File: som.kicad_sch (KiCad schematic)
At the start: 29 parts, among them J15 Bus_DDR4_SODIMM_CUSTOM_Jetson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, M1 Jetson-Orin-NX-Nano, U4 NTS0102_XSON

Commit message: Init commit
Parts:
- C1, C2: LCSC Part # (none) -> C696814
- C40, C41: LCSC Part # (none) -> C85960
- D34: LCSC Part # (none) -> C145179
- D55: LCSC Part # (none) -> C5182093
- FB1: LCSC Part # (none) -> ---
- J15: LCSC Part # (none) -> C2766246
- R1, R11, R12, R2, R3, R4, R5: LCSC Part # (none) -> C242160
- R294: LCSC Part # (none) -> C2076845
- R80: LCSC Part # (none) -> C2076851
- S1: LCSC Part # (none) -> C221676
- U4: LCSC Part # (none) -> C2687851

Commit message: Add field Digikey Part Number. Add Chinese substitute components
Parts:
- BT1: Digikey Part # (none) -> 728-1057-ND
- C1, C2: Digikey Part # (none) -> 399-13128-1-ND
- C40, C41: Digikey Part # (none) -> 490-10697-1-ND
- D34: Digikey Part # (none) -> RB521S30T1GOSCT-ND
- D55: Digikey Part # (none) -> 296-47864-1-ND
- FB1: Digikey Part # (none) -> 732-6128-1-ND; LCSC Part # --- -> (none)
- H1, H2: Digikey Part # (none) -> 732-9774065151RCT-ND
- J15: Digikey Part # (none) -> A126764CT-ND
- R1, R11, R12, R2, R3, R4, R5: Digikey Part # (none) -> P0.0JCT-ND
- R294: Digikey Part # (none) -> CR0402-FX-2201GLFCT-ND
- R80: Digikey Part # (none) -> CR0402-FX-4701GLFCT-ND
- S1: Digikey Part # (none) -> CKN10243CT-ND
- U4: Digikey Part # (none) -> 568-5205-1-ND

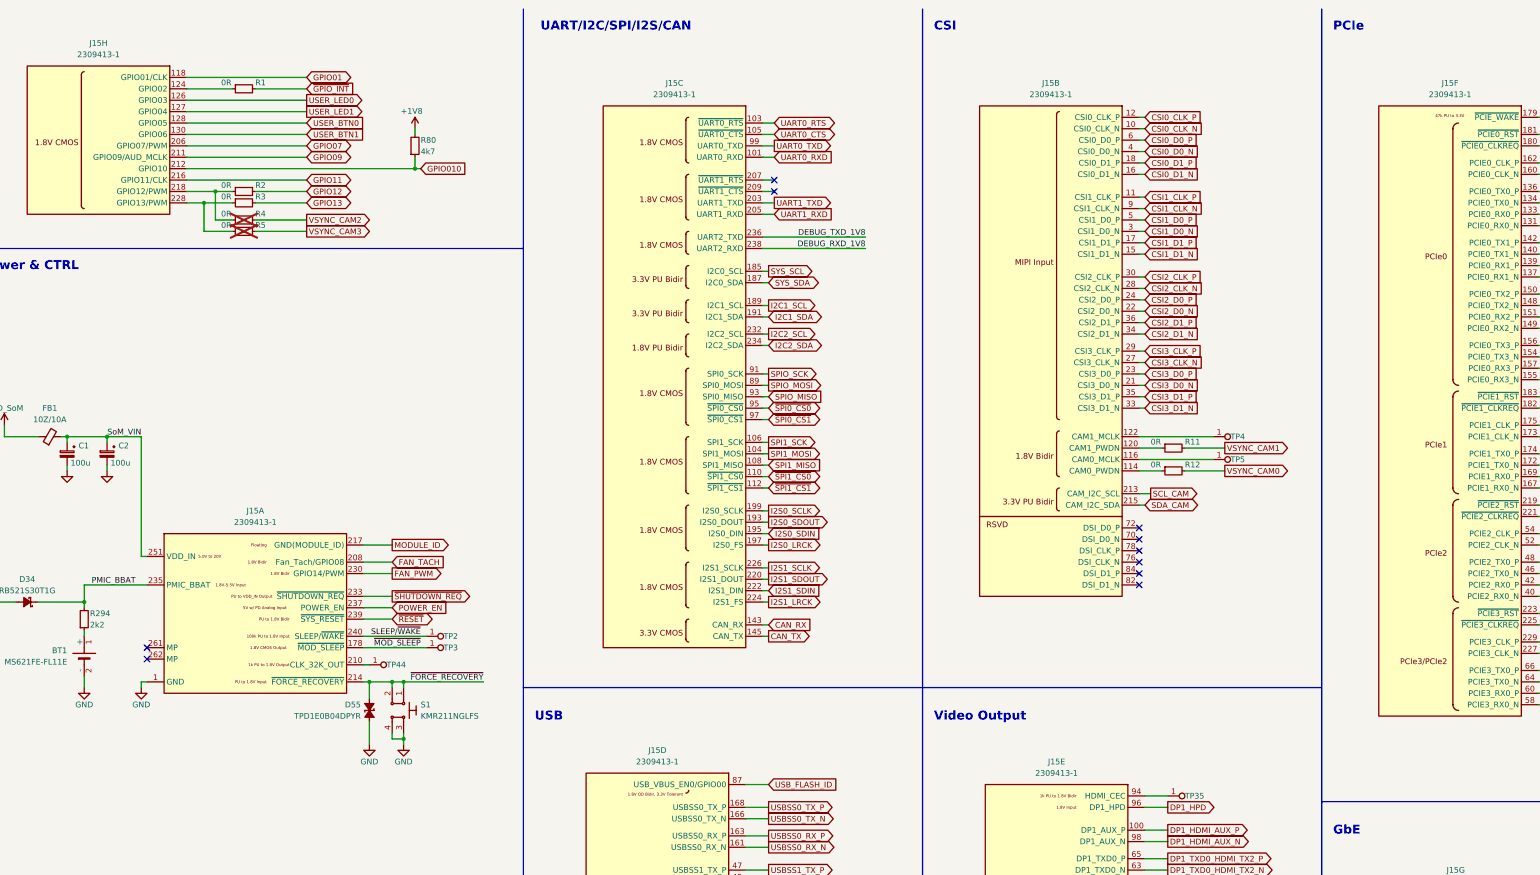
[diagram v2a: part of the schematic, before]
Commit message: Update: reorganized schematic layout for Jetson Orin Baseboard
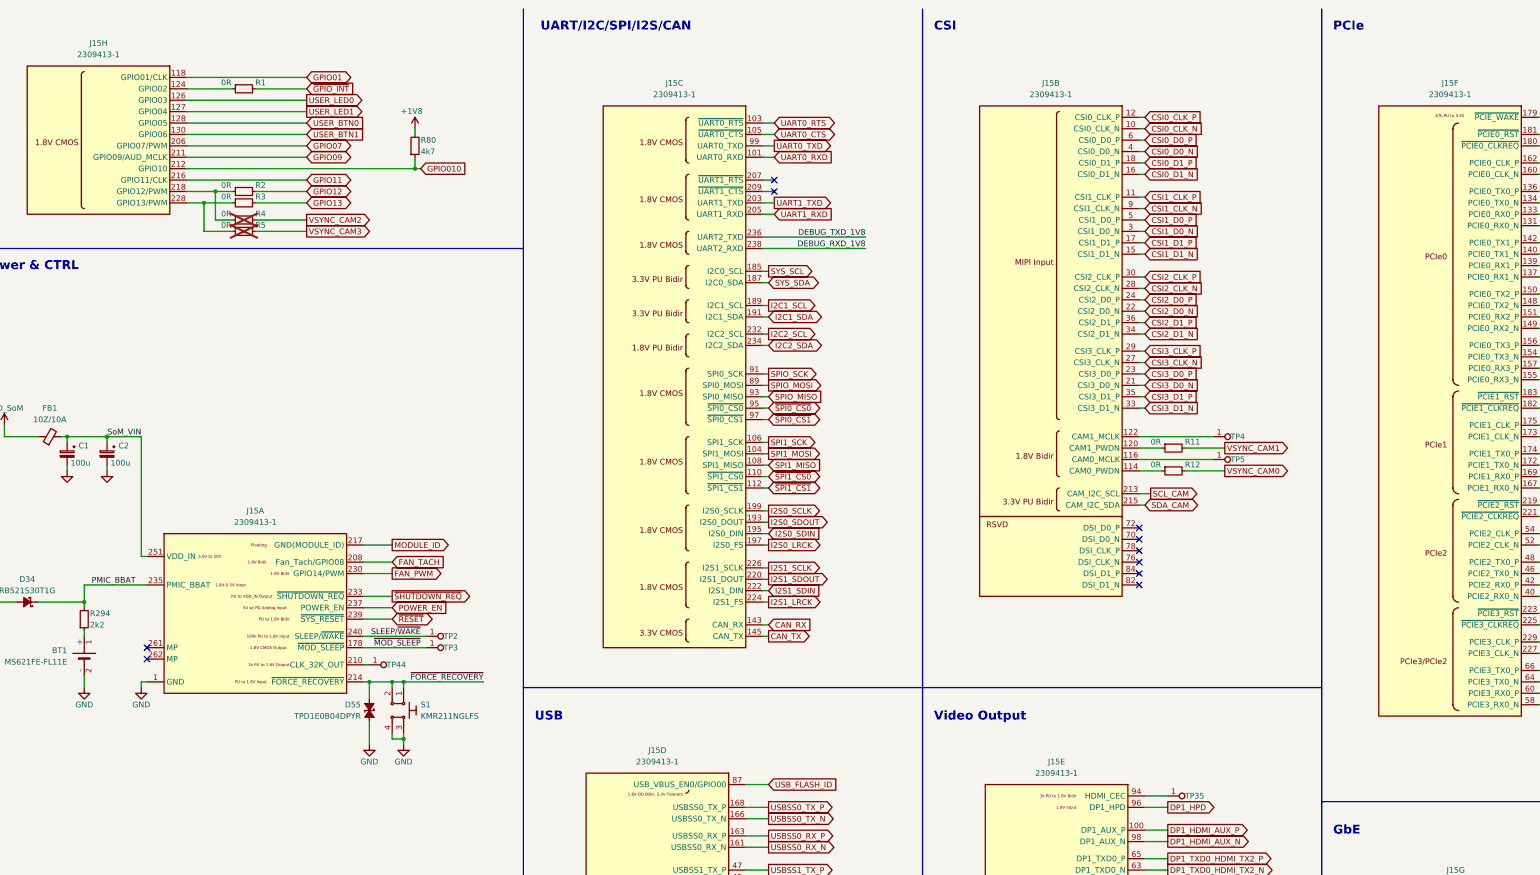
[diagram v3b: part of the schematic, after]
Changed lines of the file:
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@@
 (kicad_sch
-	(version 20231120)
+	(version 20250114)
 	(generator "eeschema")
-	(generator_version "8.0")
+	(generator_version "9.0")
 	(paper "A3")
 	(title_block
@@
 		(comment 1 "www.antmicro.com")
 	)
+	(text "DEBUG UART LEVEL SHIFTER"
+		(exclude_from_sim no)
+		(at 62.23 227.33 0)
+		(effects
+			(font
+				(size 1.27 1.27)
+				(thickness 0.254)
+				(bold yes)
+			)
+			(justify left bottom)
+		)
+	)
+	(text "CSI"
+		(exclude_from_sim no)
+		(at 231.14 19.05 0)
+		(effects
+			(font
+				(size 2 2)
+				(thickness 0.508)
+				(bold yes)
+			)
+			(justify left bottom)
+		)
+	)
+	(text "Video Output"
+		(exclude_from_sim no)
+		(at 231.14 172.72 0)
+		(effects
+			(font
+				(size 2 2)
+				(thickness 0.508)
+				(bold yes)
+			)
+			(justify left bottom)
+		)
+	)
+	(text "Power & CTRL"
+		(exclude_from_sim no)
+		(at 19.05 72.39 0)
+		(effects
+			(font
+				(size 2 2)
+				(thickness 0.508)
+				(bold yes)
+			)
+			(justify left bottom)
+		)
+	)
+	(text "UART/I2C/SPI/I2S/CAN"
+		(exclude_from_sim no)
+		(at 143.51 19.05 0)
+		(effects
+			(font
+				(size 2 2)
+				(thickness 0.508)
+				(bold yes)
+			)
+			(justify left bottom)
+		)
+	)
+	(text "PCIe"
+		(exclude_from_sim no)
+		(at 320.04 19.05 0)
+		(effects
+			(font
+				(size 2 2)
+				(thickness 0.508)
+				(bold yes)
+			)
+			(justify left bottom)
+		)
+	)
+	(text "GbE"
+		(exclude_from_sim no)
+		(at 320.04 198.12 0)
+		(effects
+			(font
+				(size 2 2)
+				(thickness 0.508)
+				(bold yes)
+			)
+			(justify left bottom)
+		)
+	)
+	(text "USB"
+		(exclude_from_sim no)
+		(at 142.24 172.72 0)
+		(effects
+			(font
+				(size 2 2)
+				(thickness 0.508)
+				(bold yes)
+			)
+			(justify left bottom)
+		)
+	)
+	(text "GPIO"
+		(exclude_from_sim no)
+		(at 13.97 19.05 0)
+		(effects
+			(font
+				(size 2 2)
+				(thickness 0.508)
+				(bold yes)
+			)
+			(justify left bottom)
+		)
+	)
+	(text "Miscellaneous"
+		(exclude_from_sim no)
+		(at 64.77 223.52 0)
+		(effects
+			(font
+				(size 2 2)
+				(thickness 0.508)
+				(bold yes)
+			)
+			(justify left bottom)
+		)
+	)
 	(junction
 		(at 68.58 57.15)
@@
 		)
 	)
-	(text "DEBUG UART LEVEL SHIFTER"
-		(exclude_from_sim no)
-		(at 62.23 227.33 0)
-		(effects
-			(font
-				(size 1.27 1.27)
-				(thickness 0.254)
-				(bold yes)
-			)
-			(justify left bottom)
-		)
-	)
-	(text "CSI"
-		(exclude_from_sim no)
-		(at 231.14 19.05 0)
-		(effects
-			(font
-				(size 2 2)
-				(thickness 0.508)
-				(bold yes)
-			)
-			(justify left bottom)
-		)
-	)
-	(text "Video Output"
-		(exclude_from_sim no)
-		(at 231.14 172.72 0)
-		(effects
-			(font
-				(size 2 2)
-				(thickness 0.508)
-				(bold yes)
-			)
-			(justify left bottom)
-		)
-	)
-	(text "Power & CTRL"
-		(exclude_from_sim no)
-		(at 19.05 72.39 0)
-		(effects
-			(font
-				(size 2 2)
-				(thickness 0.508)
-				(bold yes)
-			)
-			(justify left bottom)
-		)
-	)
-	(text "UART/I2C/SPI/I2S/CAN"
-		(exclude_from_sim no)
-		(at 143.51 19.05 0)
-		(effects
-			(font
-				(size 2 2)
-				(thickness 0.508)
-				(bold yes)
-			)
-			(justify left bottom)
-		)
-	)
-	(text "PCIe"
-		(exclude_from_sim no)
-		(at 320.04 19.05 0)
-		(effects
-			(font
-				(size 2 2)
-				(thickness 0.508)
-				(bold yes)
-			)
-			(justify left bottom)
-		)
-	)
-	(text "GbE"
-		(exclude_from_sim no)
-		(at 320.04 198.12 0)
-		(effects
-			(font
-				(size 2 2)
-				(thickness 0.508)
-				(bold yes)
-			)
-			(justify left bottom)
-		)
-	)
-	(text "USB"
-		(exclude_from_sim no)
-		(at 142.24 172.72 0)
-		(effects
-			(font
-				(size 2 2)
-				(thickness 0.508)
-				(bold yes)
-			)
-			(justify left bottom)
-		)
-	)
-	(text "GPIO"
-		(exclude_from_sim no)
-		(at 13.97 19.05 0)
-		(effects
-			(font
-				(size 2 2)
-				(thickness 0.508)
-				(bold yes)
-			)
-			(justify left bottom)
-		)
-	)
-	(text "Miscellaneous"
-		(exclude_from_sim no)
-		(at 64.77 223.52 0)
-		(effects
-			(font
-				(size 2 2)
-				(thickness 0.508)
-				(bold yes)
-			)
-			(justify left bottom)
-		)
-	)
